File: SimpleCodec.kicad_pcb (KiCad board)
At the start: 4 copper layers, 59 x 95 mm, 94 parts, among them J1 RPI_ADC, J2 RP_GPIO, U1 AMS1117-5.0, U2 AMS1117-3.3, U3 MCP6002-xSN, U4 MCP6002-xSN, U5 CS4272, X1 PEDAL_COMBO_TOP

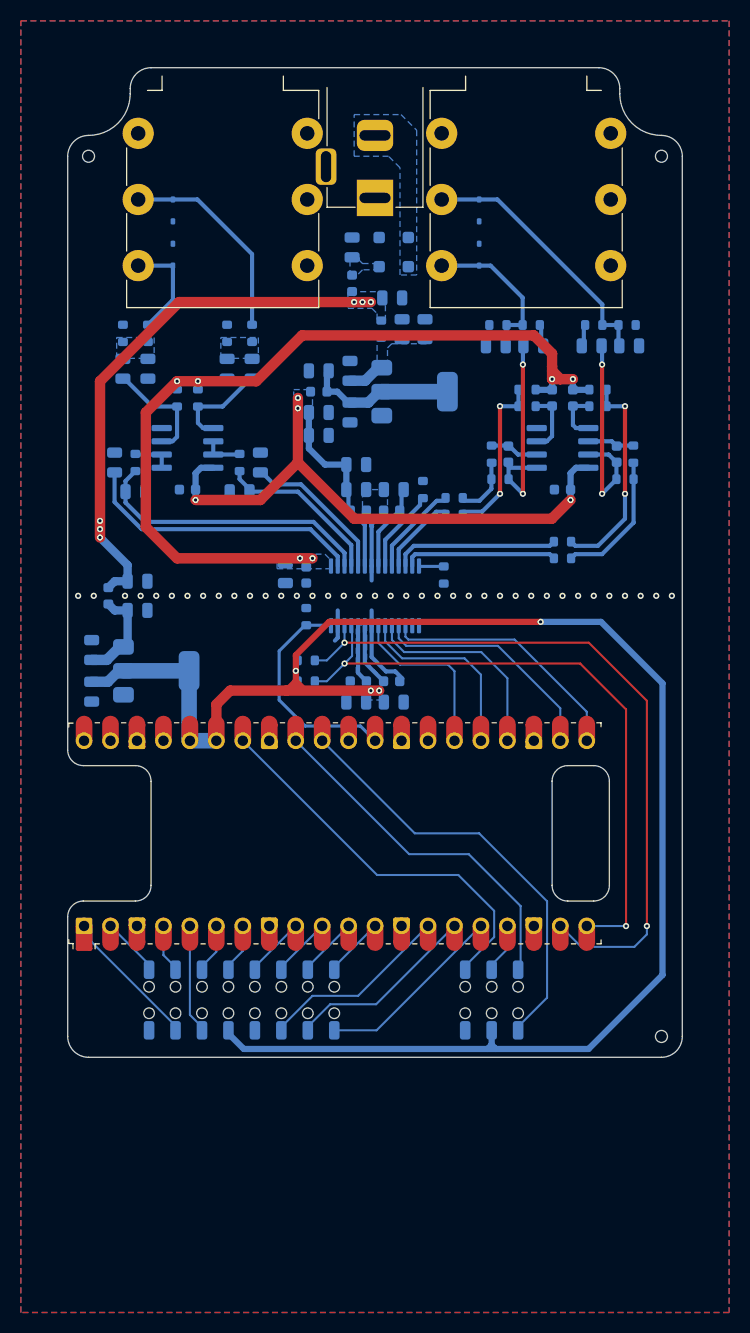
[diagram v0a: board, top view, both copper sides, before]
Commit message: Initial mounting holes
Added some minimal mounting holes.
Need to review the positioning.
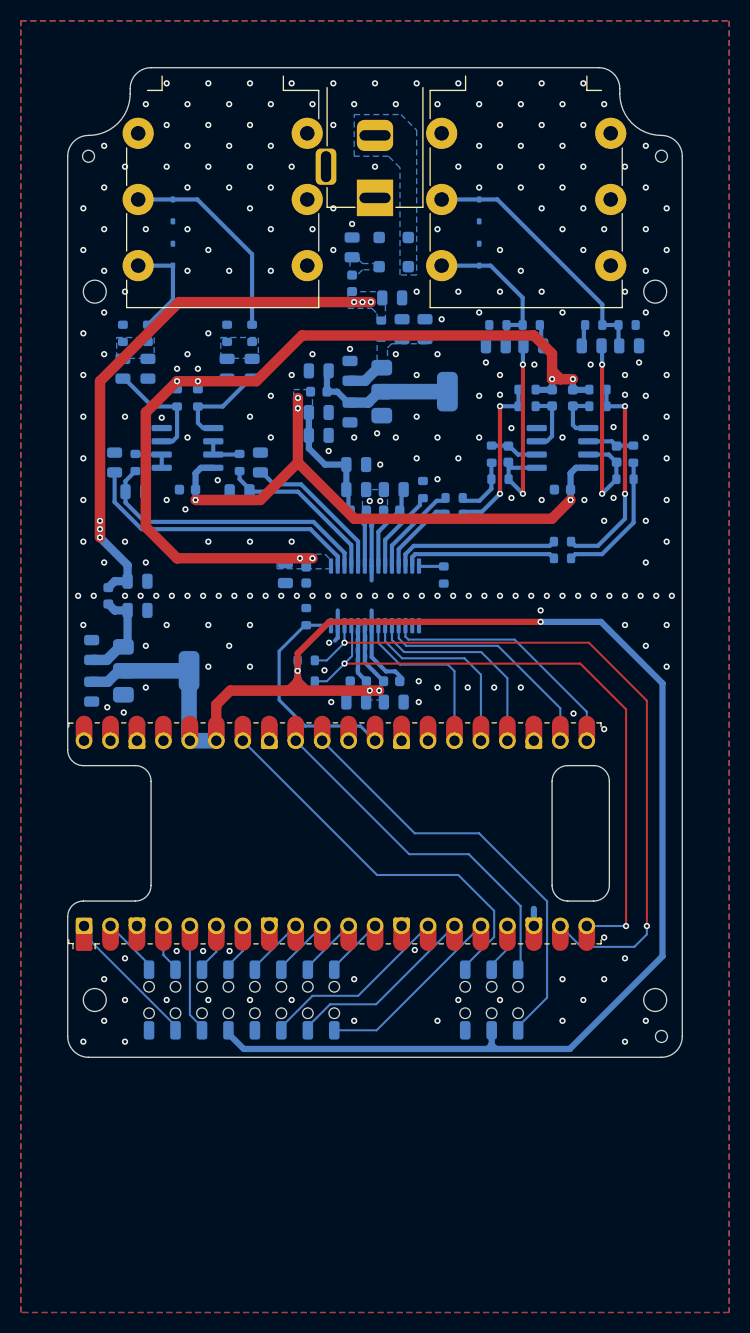
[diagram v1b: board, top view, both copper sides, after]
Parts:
- added H7: Mount, MountingHole:MountingHole_2.2mm_M2, B.Cu at (123.1, 64.0)
- added H8: Mount, MountingHole:MountingHole_2.2mm_M2, B.Cu at (176.9, 64.0)
- added REF**: MountingHole_2.2mm_M2, MountingHole:MountingHole_2.2mm_M2, B.Cu at (123.1, 132.0)
- added REF**: MountingHole_2.2mm_M2, MountingHole:MountingHole_2.2mm_M2, B.Cu at (176.9, 132.0)
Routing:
- net GND: track 20.2 -> 23.2 mm, vias 38 -> 260
- net +5VA_RAW: track 14.3 -> 13.6 mm
- net +3V3D: track 171.9 -> 171.3 mm

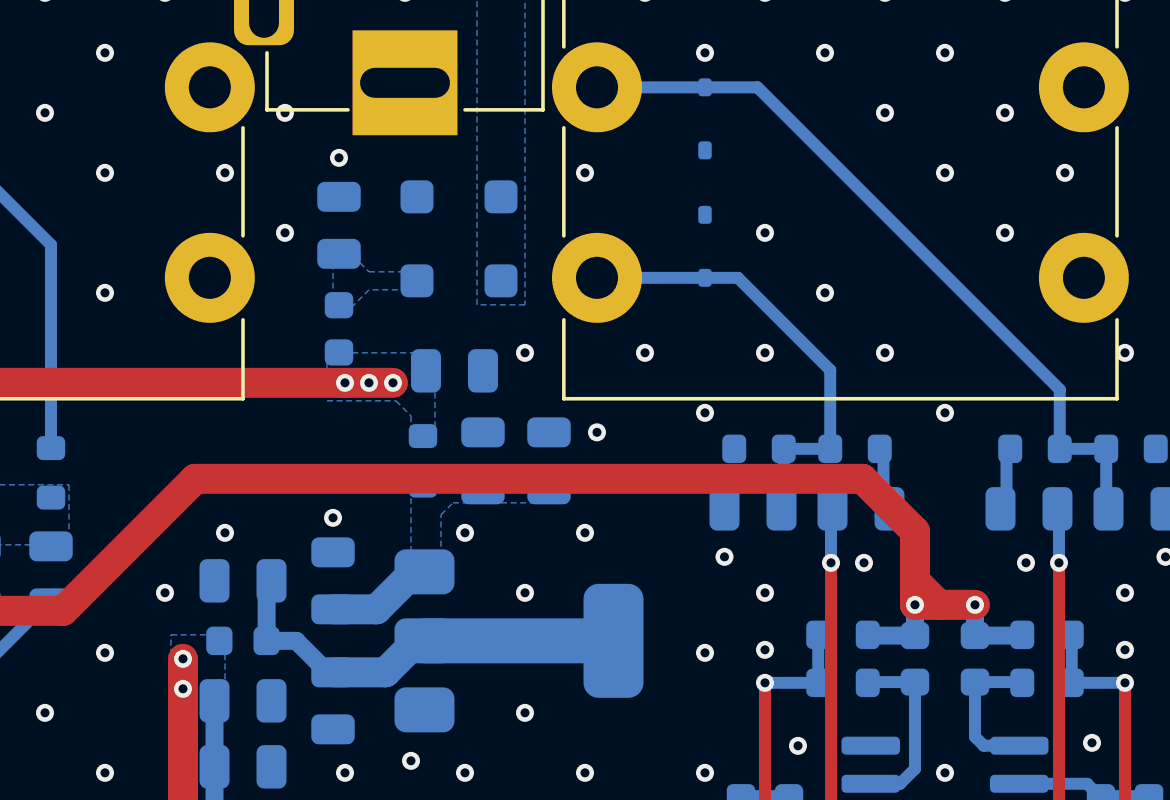
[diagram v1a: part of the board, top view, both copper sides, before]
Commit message: Silkscreen design
Updated the silkscreen for the PCB.
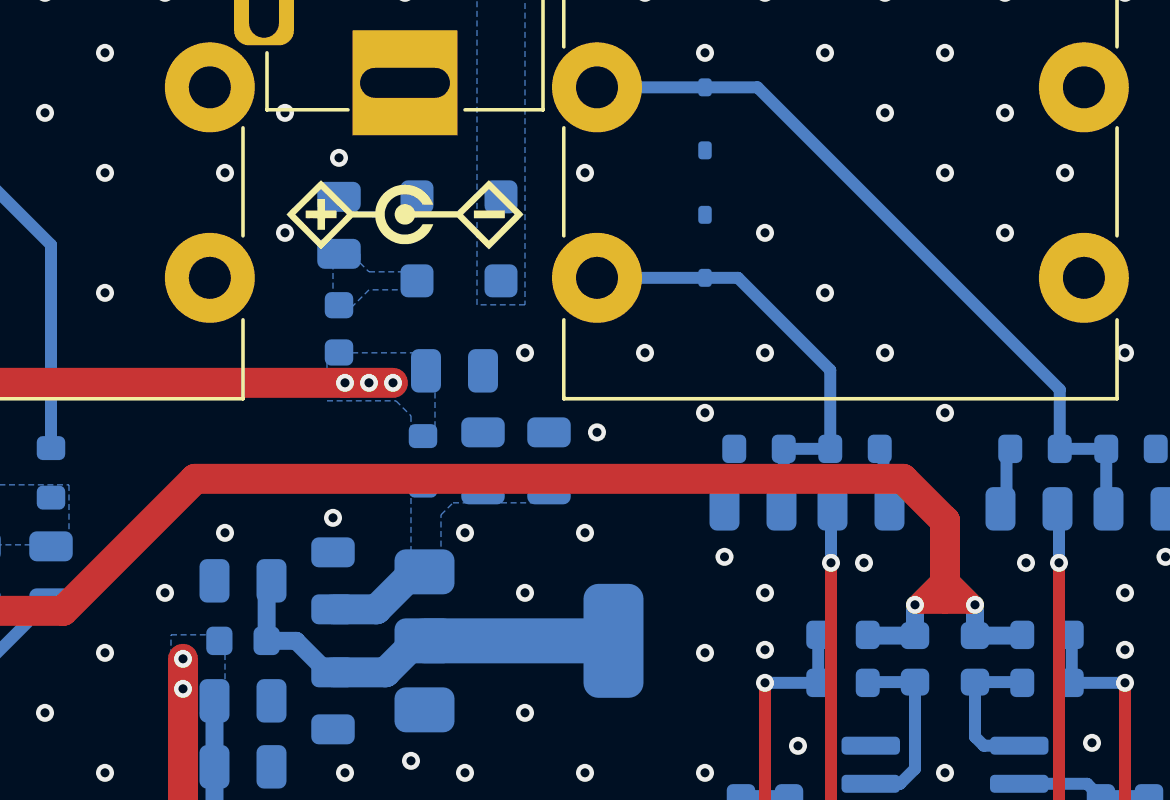
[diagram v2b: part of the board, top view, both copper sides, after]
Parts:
- removed the REF** at (123.1, 132.0)
- removed the REF** at (176.9, 132.0)
- added G***: LOGO, Logos:Polarity, F.Cu at (150.0, 59.4)
- added H10: Mount, MountingHole:MountingHole_2.2mm_M2, B.Cu at (176.9, 132.0)
- added H9: Mount, MountingHole:MountingHole_2.2mm_M2, B.Cu at (123.1, 132.0)
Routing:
- net VCOM: track 83.3 -> 88.6 mm
